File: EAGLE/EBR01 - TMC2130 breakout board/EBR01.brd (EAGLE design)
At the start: 26.7 x 25.4 mm, 27 parts

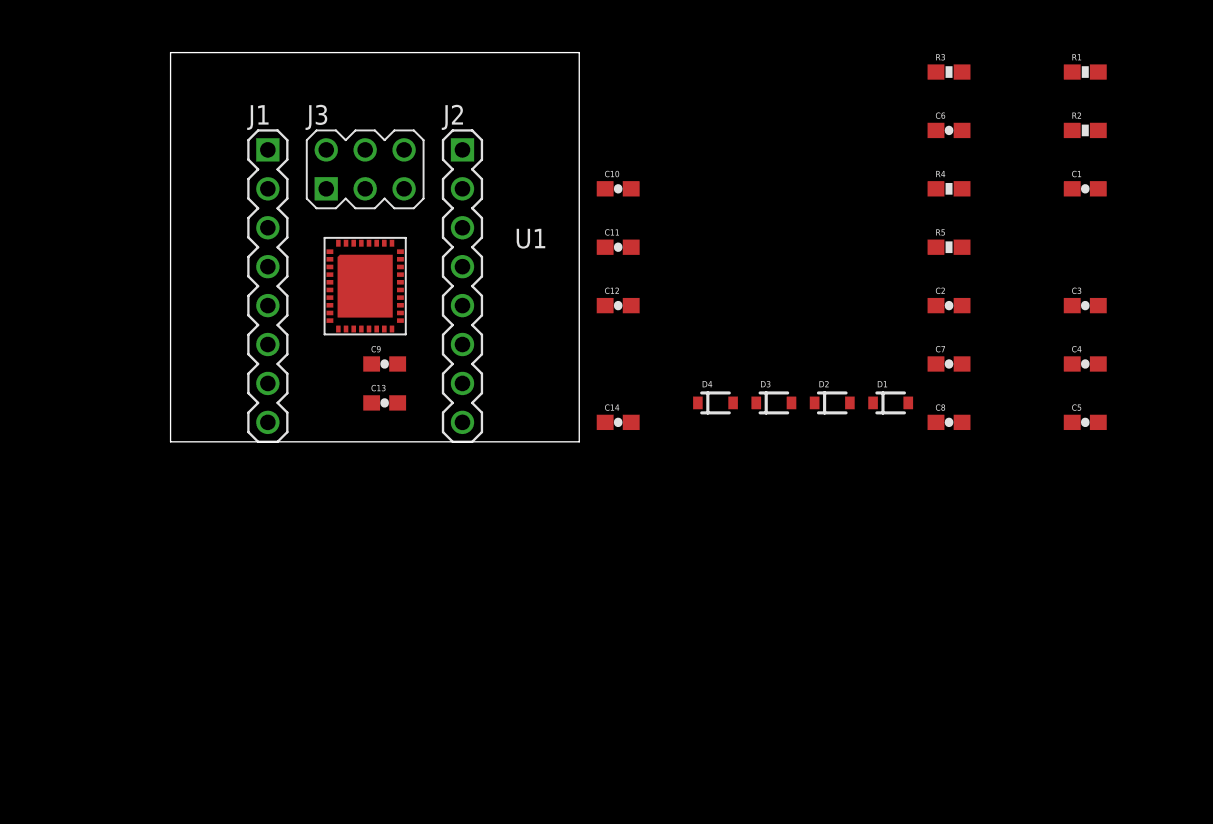
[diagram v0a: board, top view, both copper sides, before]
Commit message: Have begun replacing placeholder components with TWT Library components. Cleaning up schematic in preparation for layout.
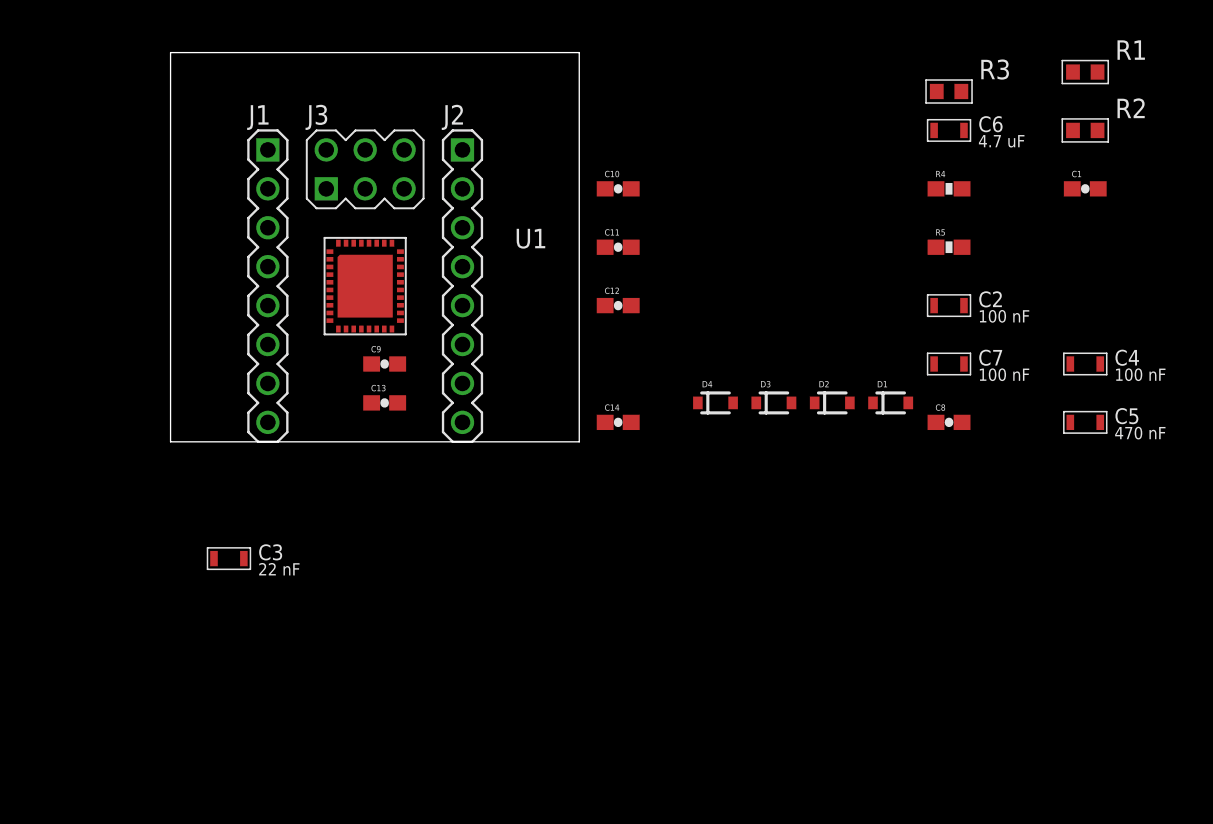
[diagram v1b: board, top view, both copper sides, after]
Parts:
- C2, C3, C4, C5, C6, C7: device SparkFun-Capacitors:0603-CAP -> TinWhiskers:C0603
- R1, R2, R3: device SparkFun-Resistors:0603-RES -> TinWhiskers:R0603
- moved C3 58.3 mm to (-1.27, -7.62)
- moved R3 1.27 mm to (45.7, 22.9)
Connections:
- net N$1: now also C3.2; no longer C3.1
- net N$5: now also C3.1; no longer C3.2
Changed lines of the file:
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@@
 <attribute name="VALUE" x="11.07" y="9.36" size="0.95" layer="27" ratio="10"/>
 </element>
-<element name="R1" library="SparkFun-Resistors" package="0603-RES" value="10K" x="54.61" y="24.13">
-<attribute name="PROD_ID" value="RES-00824" x="54.61" y="24.13" size="1.778" layer="27" display="off"/>
-</element>
-<element name="R2" library="SparkFun-Resistors" package="0603-RES" value="10K" x="54.61" y="20.32">
-<attribute name="PROD_ID" value="RES-00824" x="54.61" y="20.32" size="1.778" layer="27" display="off"/>
-</element>
+<element name="R1" library="TinWhiskers" package="R0603" value="10K" x="54.61" y="24.13"/>
+<element name="R2" library="TinWhiskers" package="R0603" value="10K" x="54.61" y="20.32"/>
 <element name="C1" library="SparkFun-Capacitors" package="0603-CAP" value="470 nF" x="54.61" y="16.51"/>
-<element name="C3" library="SparkFun-Capacitors" package="0603-CAP" value="22 nF" x="54.61" y="8.89"/>
-<element name="C4" library="SparkFun-Capacitors" package="0603-CAP" value="100 nF" x="54.61" y="5.08"/>
-<element name="C5" library="SparkFun-Capacitors" package="0603-CAP" value="470 nF" x="54.61" y="1.27"/>
-<element name="R3" library="SparkFun-Resistors" package="0603-RES" value="2R2" x="45.72" y="24.13">
-<attribute name="PROD_ID" value="RES-00824" x="45.72" y="24.13" size="1.778" layer="27" display="off"/>
-</element>
-<element name="C6" library="SparkFun-Capacitors" package="0603-CAP" value="4.7 uF" x="45.72" y="20.32"/>
+<element name="C4" library="TinWhiskers" package="C0603" value="100 nF" x="54.61" y="5.08"/>
+<element name="C5" library="TinWhiskers" package="C0603" value="470 nF" x="54.61" y="1.27"/>
+<element name="R3" library="TinWhiskers" package="R0603" value="2R2" x="45.72" y="22.86"/>
+<element name="C6" library="TinWhiskers" package="C0603" value="4.7 uF" x="45.72" y="20.32"/>
 <element name="R4" library="SparkFun-Resistors" package="0603-RES" value="1206, 1/2W" x="45.72" y="16.51">
 <attribute name="PROD_ID" value="RES-00824" x="45.72" y="16.51" size="1.778" layer="27" display="off"/>
@@
 </element>
 <element name="J3" library="!con-lstb" package="MA03-2" value="" x="7.62" y="17.78"/>
-<element name="C2" library="SparkFun-Capacitors" package="0603-CAP" value="100 nF" x="45.72" y="8.89"/>
-<element name="C7" library="SparkFun-Capacitors" package="0603-CAP" value="100 nF" x="45.72" y="5.08"/>
+<element name="C2" library="TinWhiskers" package="C0603" value="100 nF" x="45.72" y="8.89"/>
+<element name="C7" library="TinWhiskers" package="C0603" value="100 nF" x="45.72" y="5.08"/>
 <element name="C8" library="SparkFun-Capacitors" package="0603-CAP" value="100 uF" x="45.72" y="1.27"/>
 <element name="D1" library="SparkFun-DiscreteSemi" package="SOD-323" value="MSS1P6" x="41.91" y="2.54">
@@
 <element name="C13" library="SparkFun-Capacitors" package="0603-CAP" value="100nF 16V" x="8.89" y="2.54"/>
 <element name="C14" library="SparkFun-Capacitors" package="0603-CAP" value="100nF 16V" x="24.13" y="1.27"/>
+<element name="C3" library="TinWhiskers" package="C0603" value="22 nF" x="-1.27" y="-7.62"/>
 </elements>
 <signals>
@@
 <contactref element="C7" pad="1"/>
 <contactref element="C8" pad="1"/>
-<wire x1="55.46" y1="1.27" x2="55.46" y2="5.08" width="0" layer="19" extent="1-1"/>
-<wire x1="44.87" y1="5.08" x2="55.46" y2="5.08" width="0" layer="19" extent="1-1"/>
-<wire x1="44.87" y1="8.89" x2="44.87" y2="5.08" width="0" layer="19" extent="1-1"/>
-<wire x1="44.87" y1="1.27" x2="44.87" y2="5.08" width="0" layer="19" extent="1-1"/>
-<wire x1="13.97" y1="19.05" x2="44.87" y2="8.89" width="0" layer="19" extent="1-1"/>
+<wire x1="55.585" y1="1.27" x2="55.585" y2="5.08" width="0" layer="19" extent="1-1"/>
+<wire x1="44.745" y1="5.08" x2="55.585" y2="5.08" width="0" layer="19" extent="1-1"/>
+<wire x1="44.745" y1="8.89" x2="44.745" y2="5.08" width="0" layer="19" extent="1-1"/>
+<wire x1="44.87" y1="1.27" x2="44.745" y2="5.08" width="0" layer="19" extent="1-1"/>
+<wire x1="13.97" y1="19.05" x2="44.745" y2="8.89" width="0" layer="19" extent="1-1"/>
 <wire x1="8.87" y1="12.96" x2="13.97" y2="19.05" width="0" layer="19" extent="1-1"/>
 <wire x1="8.37" y1="12.96" x2="8.87" y2="12.96" width="0" layer="19" extent="1-1"/>
@@
 <contactref element="C14" pad="2"/>
 <contactref element="C13" pad="2"/>
-<wire x1="46.57" y1="20.32" x2="55.46" y2="16.51" width="0" layer="19" extent="1-1"/>
-<wire x1="44.87" y1="16.51" x2="46.57" y2="20.32" width="0" layer="19" extent="1-1"/>
+<wire x1="46.695" y1="20.32" x2="55.46" y2="16.51" width="0" layer="19" extent="1-1"/>
+<wire x1="44.87" y1="16.51" x2="46.695" y2="20.32" width="0" layer="19" extent="1-1"/>
 <wire x1="44.87" y1="12.7" x2="44.87" y2="16.51" width="0" layer="19" extent="1-1"/>
-<wire x1="46.57" y1="8.89" x2="44.87" y2="12.7" width="0" layer="19" extent="1-1"/>
-<wire x1="46.57" y1="5.08" x2="46.57" y2="8.89" width="0" layer="19" extent="1-1"/>
-<wire x1="46.57" y1="1.27" x2="46.57" y2="5.08" width="0" layer="19" extent="1-1"/>
-<wire x1="53.76" y1="1.27" x2="46.57" y2="1.27" width="0" layer="19" extent="1-1"/>
+<wire x1="46.695" y1="8.89" x2="44.87" y2="12.7" width="0" layer="19" extent="1-1"/>
+<wire x1="46.695" y1="5.08" x2="46.695" y2="8.89" width="0" layer="19" extent="1-1"/>
+<wire x1="46.57" y1="1.27" x2="46.695" y2="5.08" width="0" layer="19" extent="1-1"/>
+<wire x1="53.635" y1="1.27" x2="46.57" y2="1.27" width="0" layer="19" extent="1-1"/>
 <wire x1="24.98" y1="16.51" x2="44.87" y2="16.51" width="0" layer="19" extent="1-1"/>
 <wire x1="24.98" y1="12.7" x2="24.98" y2="16.51" width="0" layer="19" extent="1-1"/>
@@
 <contactref element="U1" pad="20"/>
 <contactref element="R2" pad="1"/>
-<wire x1="9.92" y1="8.41" x2="53.76" y2="20.32" width="0" layer="19" extent="1-1"/>
+<wire x1="9.92" y1="8.41" x2="53.81" y2="20.32" width="0" layer="19" extent="1-1"/>
 </signal>
 <signal name="N$7">
 <contactref element="U1" pad="21"/>
 <contactref element="R1" pad="1"/>
-<wire x1="9.92" y1="8.91" x2="53.76" y2="24.13" width="0" layer="19" extent="1-1"/>
+<wire x1="9.92" y1="8.91" x2="53.81" y2="24.13" width="0" layer="19" extent="1-1"/>
 </signal>
 <signal name="5VOUT">
@@
 <contactref element="C1" pad="1"/>
 <contactref element="R3" pad="1"/>
-<wire x1="44.87" y1="24.13" x2="53.76" y2="16.51" width="0" layer="19" extent="1-1"/>
-<wire x1="9.92" y1="10.91" x2="44.87" y2="24.13" width="0" layer="19" extent="1-1"/>
+<wire x1="44.92" y1="22.86" x2="53.76" y2="16.51" width="0" layer="19" extent="1-1"/>
+<wire x1="9.92" y1="10.91" x2="44.92" y2="22.86" width="0" layer="19" extent="1-1"/>
 </signal>
 <signal name="VCC">
@@
 <contactref element="R3" pad="2"/>
 <contactref element="C6" pad="1"/>
-<wire x1="44.87" y1="20.32" x2="46.57" y2="24.13" width="0" layer="19" extent="1-1"/>
-<wire x1="9.92" y1="11.41" x2="44.87" y2="20.32" width="0" layer="19" extent="1-1"/>
+<wire x1="44.745" y1="20.32" x2="46.52" y2="22.86" width="0" layer="19" extent="1-1"/>
+<wire x1="9.92" y1="11.41" x2="44.745" y2="20.32" width="0" layer="19" extent="1-1"/>
 <wire x1="5.32" y1="8.91" x2="9.92" y2="11.41" width="0" layer="19" extent="1-1"/>
 </signal>
 <signal name="N$1">
-<contactref element="C3" pad="1"/>
 <contactref element="U1" pad="28"/>
-<wire x1="9.92" y1="12.41" x2="53.76" y2="8.89" width="0" layer="19" extent="1-1"/>
+<contactref element="C3" pad="2"/>
+<wire x1="-0.295" y1="-7.62" x2="9.92" y2="12.41" width="0" layer="19" extent="1-1"/>
 </signal>
 <signal name="N$5">
 <contactref element="U1" pad="27"/>
-<contactref element="C3" pad="2"/>
-<wire x1="9.92" y1="11.91" x2="55.46" y2="8.89" width="0" layer="19" extent="1-1"/>
+<contactref element="C3" pad="1"/>
+<wire x1="-2.245" y1="-7.62" x2="9.92" y2="11.91" width="0" layer="19" extent="1-1"/>
 </signal>
 <signal name="N$8">
 <contactref element="U1" pad="29"/>
 <contactref element="C4" pad="1"/>
-<wire x1="9.37" y1="12.96" x2="53.76" y2="5.08" width="0" layer="19" extent="1-1"/>
+<wire x1="9.37" y1="12.96" x2="53.635" y2="5.08" width="0" layer="19" extent="1-1"/>
 </signal>
 <signal name="N$3">

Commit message: Updated all components to reflect accurate devices. Smashed most of the parts that required it. The only remaining issues with the schematic are the external voltage regulator and a couple unconnected connections which require clarification.
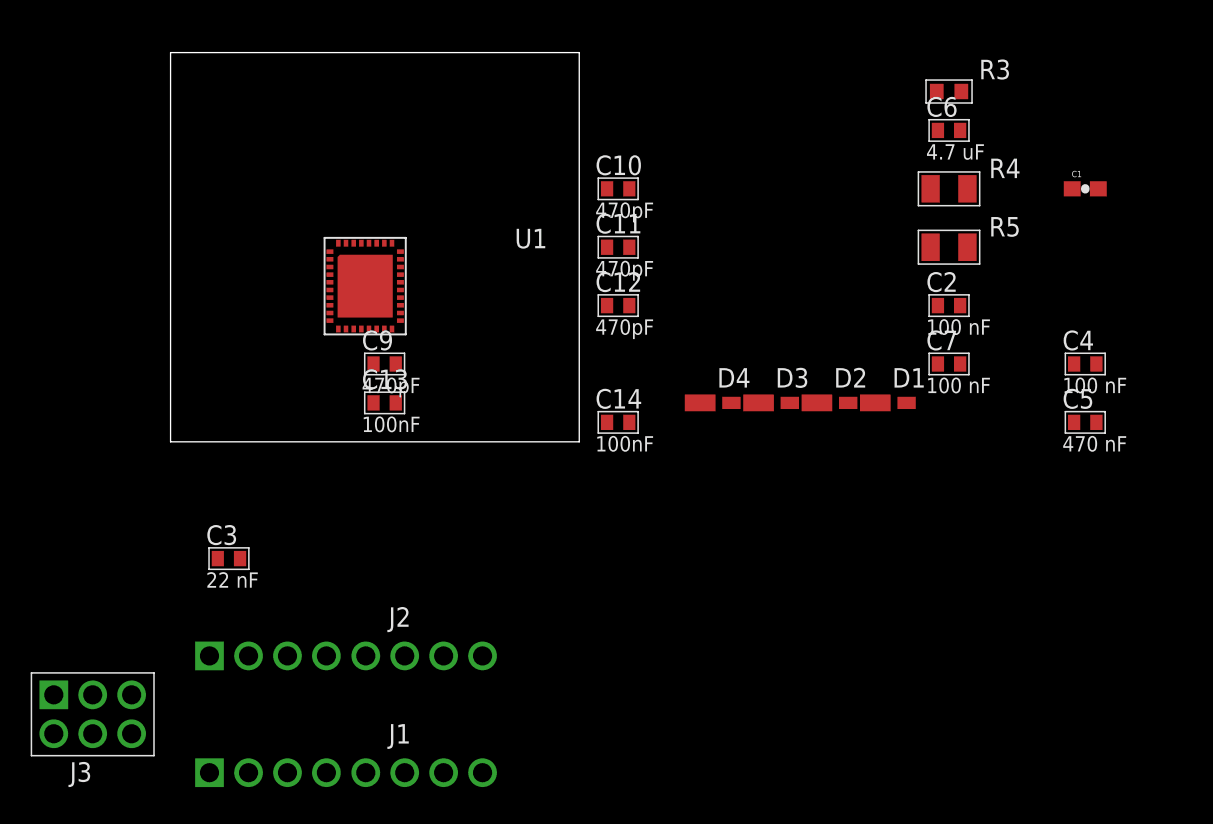
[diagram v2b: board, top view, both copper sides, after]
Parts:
- removed C8: 100 uF, SparkFun-Capacitors:0603-CAP
- removed R1, R2: 10K, TinWhiskers:R0603
- C10, C11, C12, C9: value 470pF 100V -> 470pF; device SparkFun-Capacitors:0603-CAP -> TinWhiskers:C0603
- C13, C14: value 100nF 16V -> 100nF; device SparkFun-Capacitors:0603-CAP -> TinWhiskers:C0603
- D1, D2, D3, D4: device SparkFun-DiscreteSemi:SOD-323 -> TinWhiskers:MICRO-SMP
- J1, J2: value (none) -> CPL-CON-HEADER-0.1IN-8P-M; device !con-lstb:MA08-1 -> TinWhiskers:CON-HDR-8POS-MALE
- J3: value (none) -> CPL-CON-HEADER-0.1IN-2X3P-M; device !con-lstb:MA03-2 -> TinWhiskers:CON-HDR-2X3P
- R4, R5: value 1206, 1/2W -> 0.22; device SparkFun-Resistors:0603-RES -> TinWhiskers:R1206
- moved J3 39.8 mm to (-10.2, -17.8)
- moved J1 32.2 mm to (6.35, -21.6), turned to 0 degrees
- moved J2 25.3 mm to (6.35, -14.0), turned to 0 degrees
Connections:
- removed net N$6: R2.1, U1.20
- removed net N$7: R1.1, U1.21
- net 1A: now also D3.NEG; no longer D3.C
- net 1B: now also D4.NEG; no longer D4.C
- net 2A: now also D2.NEG; no longer D2.C
- net 2B: now also D1.NEG; no longer D1.C
- net GND: no longer C8.2
- net N$3: now also D1.POS, D2.POS; no longer D1.A, D2.A
- net N$4: now also D3.POS, D4.POS; no longer D3.A, D4.A
- net VMOT: no longer C8.1
